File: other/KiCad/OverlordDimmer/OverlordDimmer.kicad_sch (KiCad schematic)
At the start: 103 parts, among them J1 Connector_Screw_Terminal_01x09, J2 USB_B, J3 DE15_Plug_HighDensity_Mountin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, J4 Connector_Screw_Terminal_01x09, J6 Conn_01x12_Pin, Q43 2SC4061KT146N, Q44 BC817, Q45 2SC4061KT146N, U12 4N35, U13 LM317_SOT-223, U14 ESP32S3-Wroom, U4 SN65HVD230

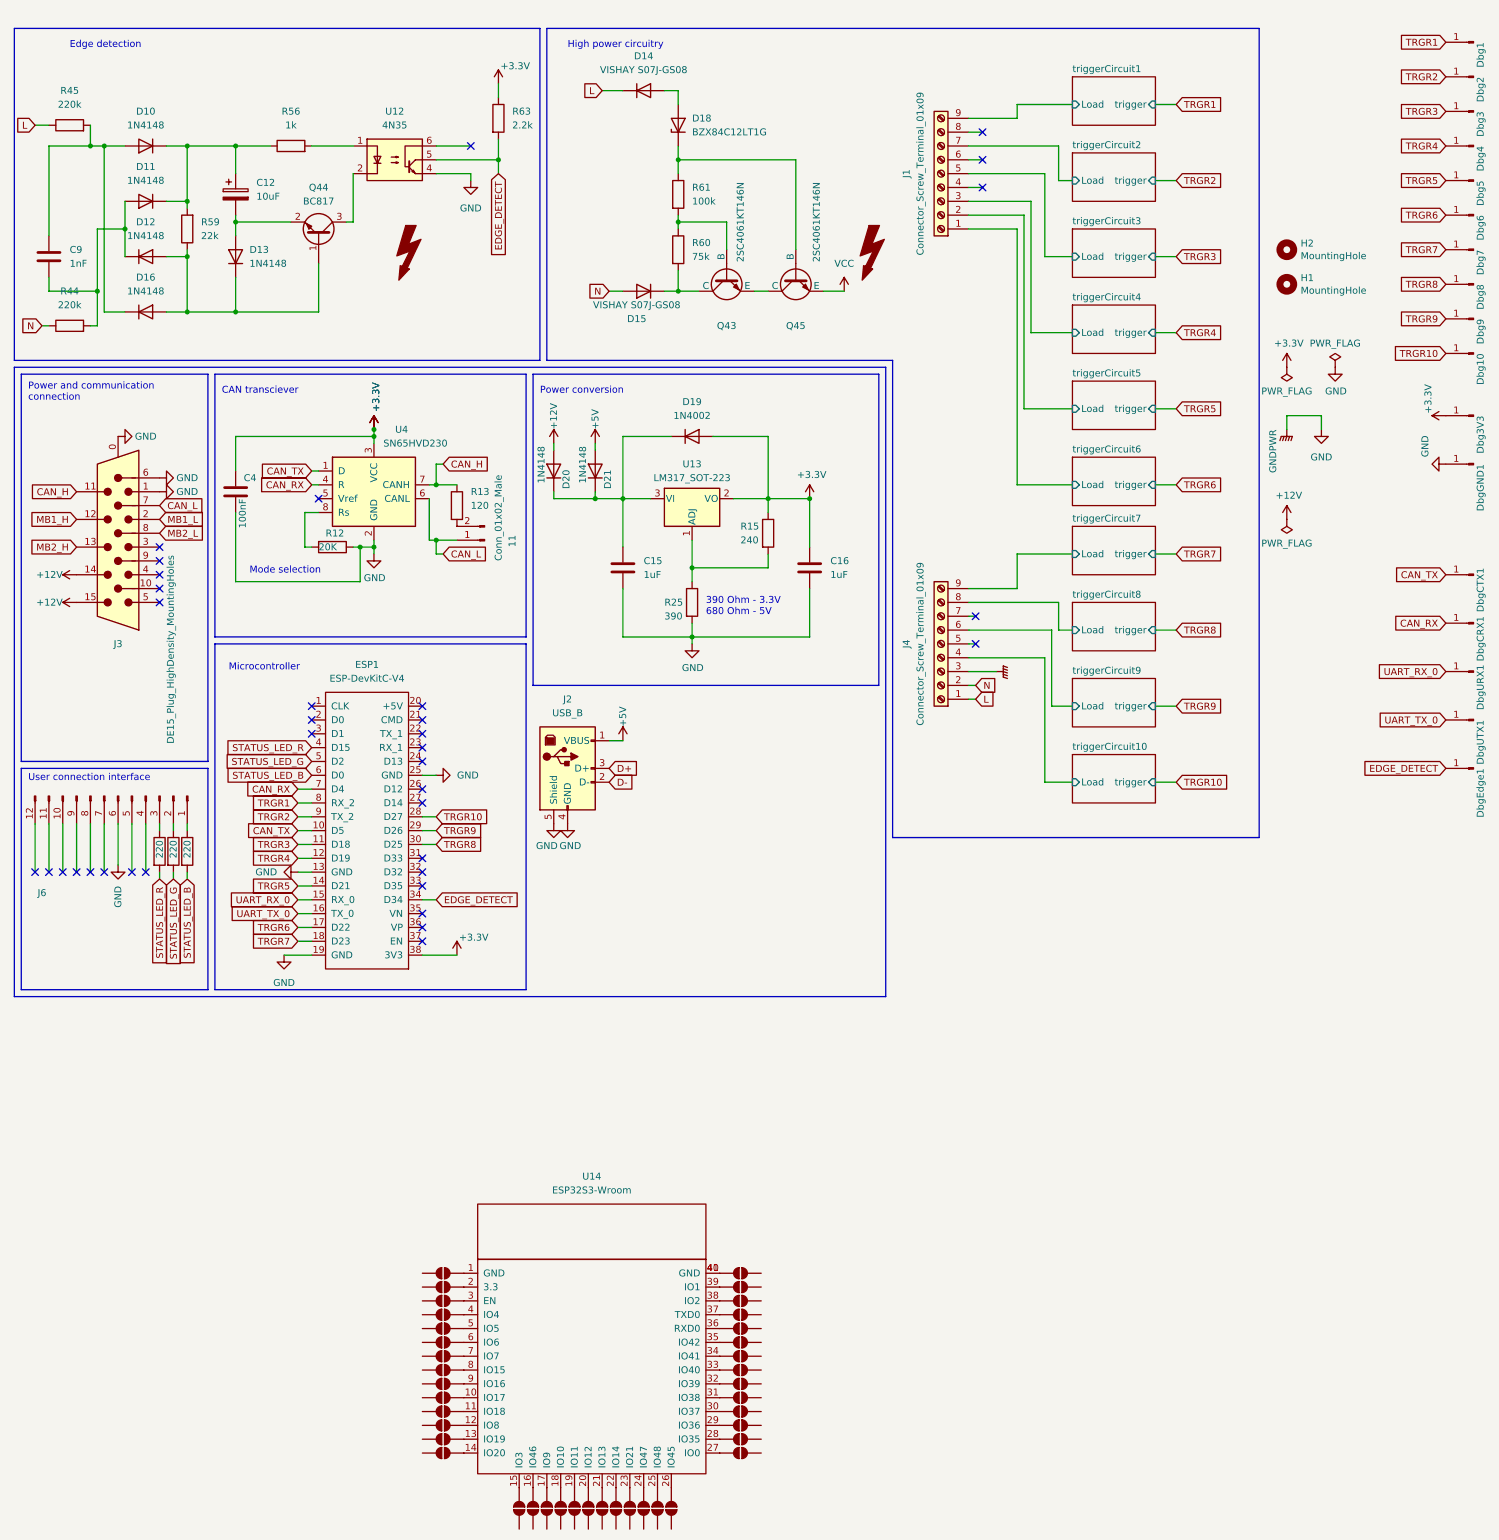
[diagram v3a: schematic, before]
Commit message: Modified for S3 migration Prepared PCB for final inspection
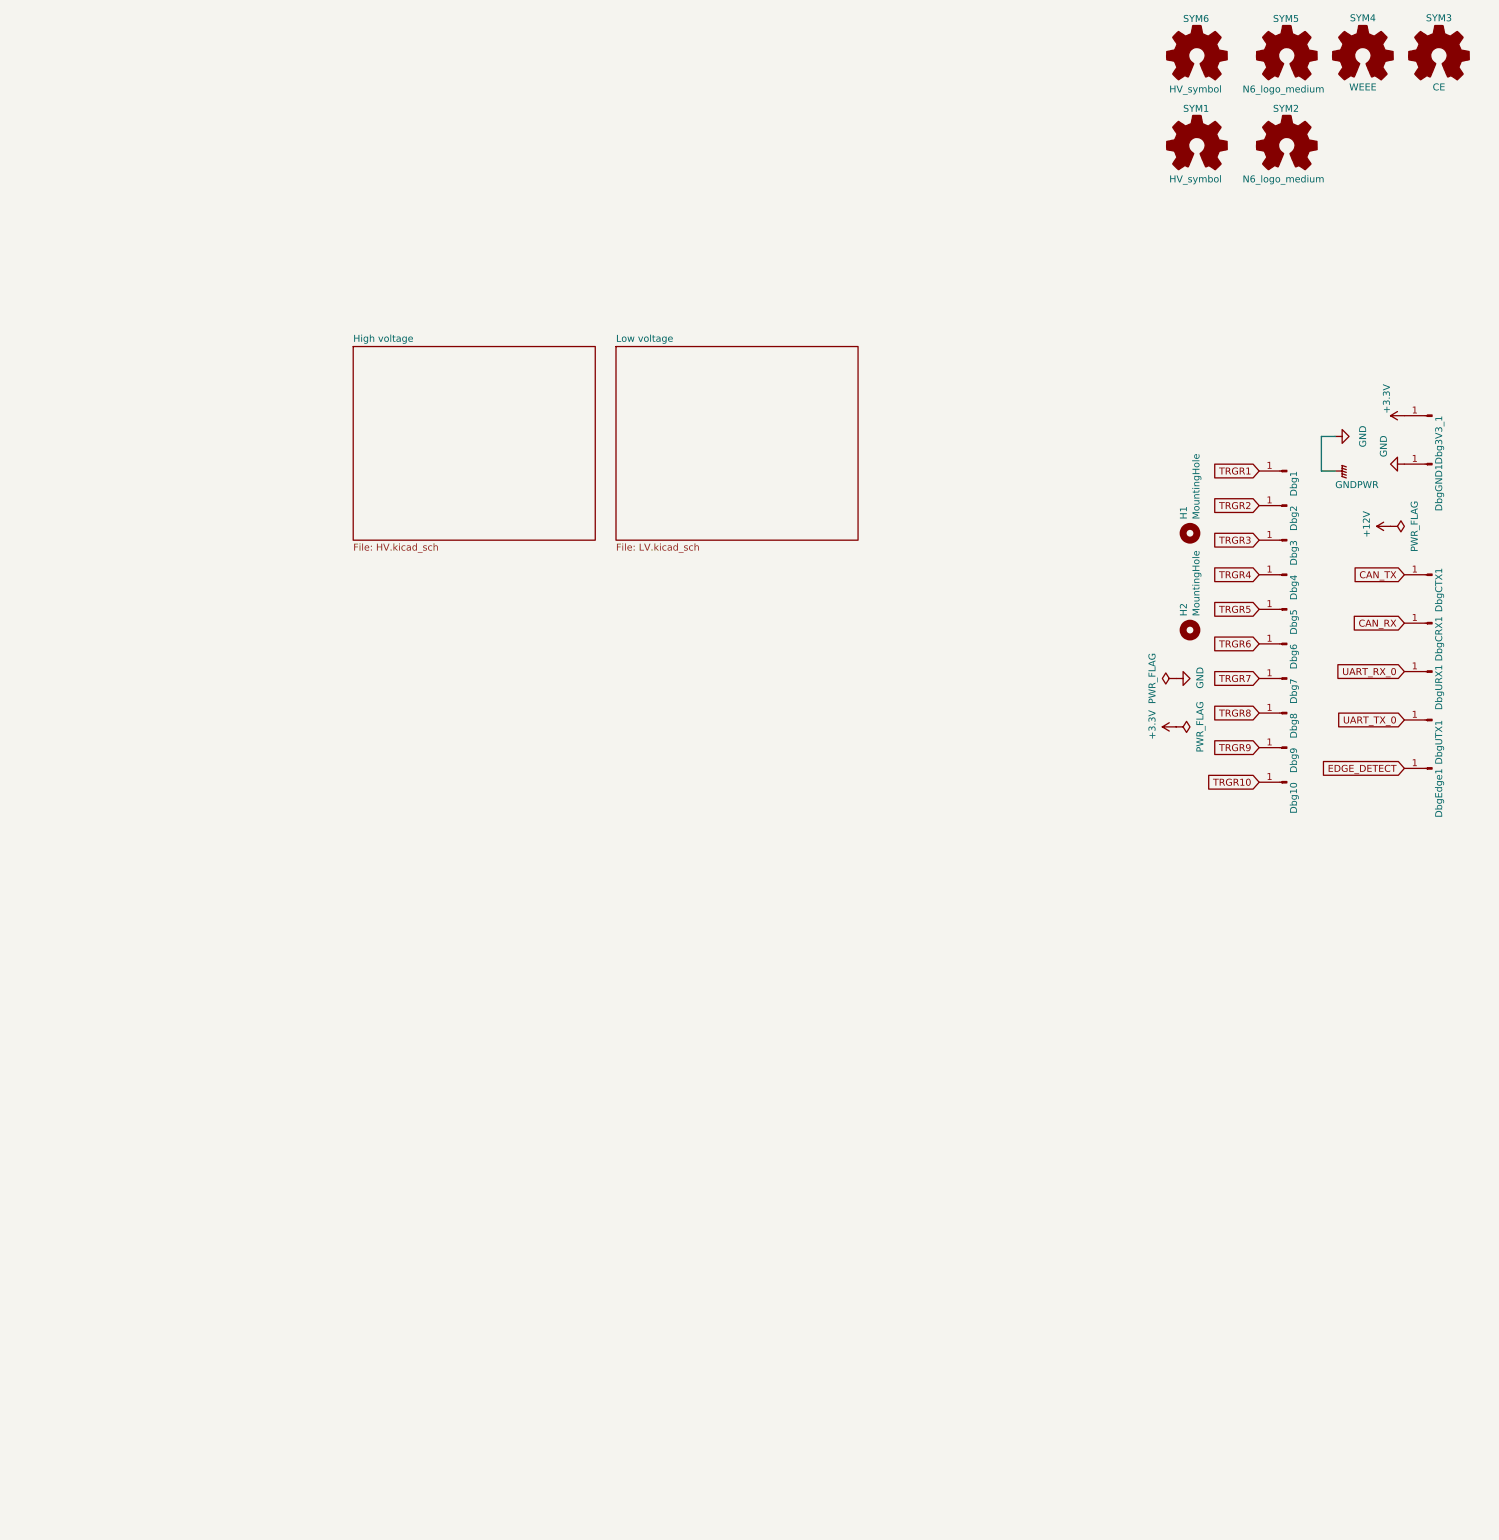
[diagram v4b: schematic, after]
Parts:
- removed 11: Conn_01x02_Male, Connector_PinHeader_2.54mm:PinHeader_1x02_P2.54mm_Vertical, symbol Connector:Conn_01x02_Pin
- removed C12: 10uF, Capacitor_THT:CP_Radial_D4.0mm_P1.50mm, symbol Device:C_Polarized
- removed C15, C16: 1uF, Capacitor_SMD:C_0402_1005Metric_Pad0.74x0.62mm_HandSolder, symbol Device:C
- removed C4: 100nF, Capacitor_THT:C_Disc_D6.0mm_W2.5mm_P5.00mm, symbol Device:C
- removed C9: 1nF, Capacitor_THT:C_Disc_D5.0mm_W2.5mm_P2.50mm, symbol Device:C
- removed D10, D11, D12, D13, D16, D20, D21: 1N4148, Diode_THT:D_DO-35_SOD27_P7.62mm_Horizontal, symbol Diode:1N4148
- removed D14, D15: VISHAY S07J-GS08, Diode_SMD:D_SMF, symbol Device:D
- removed D18: BZX84C12LT1G, Package_TO_SOT_SMD:SOT-23, symbol Diode:BZX84Cxx
- removed D19: 1N4002, Diode_THT:D_DO-41_SOD81_P2.54mm_Vertical_KathodeUp, symbol Device:D
- removed ESP1: ESP-DevKitC-V4, Overlord:ESP32-DevKitC-V4, symbol 74HC251D,653:ESP-DevKitC-V4
- removed J1, J4: Connector_Screw_Terminal_01x09, TerminalBlockCustom:TerminalBlock_9_5.08mm, symbol Overlord-cache:Connector_Screw_Terminal_01x09
- removed J2: USB_B, Connector_USB:USB_B_Lumberg_2411_02_Horizontal, symbol Connector:USB_B
- removed J3: DE15_Plug_HighDensity_MountingHoles, DSUB-15_Male_Horizontal_P2.77x2.84mm_EdgePinOffset7.70mm_Housed_MountingHolesOffset9.12mm, symbol Connector:DE15_Plug_HighDensity_MountingHoles
- removed J6: Conn_01x12_Pin, Connector_Molex:Molex_Picoflex_90325-0012_2x06_P1.27mm_Vertical, symbol Connector:Conn_01x12_Pin
- removed JP1, JP10, JP11, JP12, JP13, JP14, JP15, JP16, JP17, JP18, JP19, JP2, JP20, JP21, JP22, JP23, JP24, JP25, JP26, JP27, JP28, JP29, JP3, JP30, JP31, JP32, JP33, JP34, JP35, JP36, JP37, JP38, JP39, JP4, JP40, JP5, JP6, JP7, JP8, JP9: SolderJumper_2_Open, Jumper:SolderJumper-2_P1.3mm_Open_RoundedPad1.0x1.5mm, symbol Jumper:SolderJumper_2_Open
- removed Q43, Q45: 2SC4061KT146N, Package_TO_SOT_SMD:SC-59_Handsoldering, symbol Simulation_SPICE:NPN
- removed Q44: BC817, Package_TO_SOT_SMD:SOT-23, symbol Transistor_BJT:BC817
- removed R12: 20K, Resistor_SMD:R_0402_1005Metric_Pad0.72x0.64mm_HandSolder, symbol Device:R
- removed R13: 120, Resistor_SMD:R_0402_1005Metric_Pad0.72x0.64mm_HandSolder, symbol Device:R
- removed R15: 240, Resistor_SMD:R_1206_3216Metric_Pad1.30x1.75mm_HandSolder, symbol Device:R
- removed R25: 390, Resistor_SMD:R_1206_3216Metric_Pad1.30x1.75mm_HandSolder, symbol Device:R
- removed R44, R45: 220k, Resistor_SMD:R_0805_2012Metric_Pad1.20x1.40mm_HandSolder, symbol Device:R
- removed R56: 1k, Resistor_SMD:R_0805_2012Metric_Pad1.20x1.40mm_HandSolder, symbol Device:R
- removed R59: 22k, Resistor_SMD:R_0805_2012Metric_Pad1.20x1.40mm_HandSolder, symbol Device:R
- removed R60: 75k, Resistor_SMD:R_0805_2012Metric_Pad1.20x1.40mm_HandSolder, symbol Device:R
- removed R61: 100k, Resistor_SMD:R_0805_2012Metric_Pad1.20x1.40mm_HandSolder, symbol Device:R
- removed R63: 2.2k, Resistor_SMD:R_0805_2012Metric_Pad1.20x1.40mm_HandSolder, symbol Device:R
- removed R64, R65, R66: 220, Resistor_SMD:R_0805_2012Metric_Pad1.20x1.40mm_HandSolder, symbol Device:R
- removed U12: 4N35, Package_DIP:DIP-6_W7.62mm, symbol Isolator:4N35
- removed U13: LM317_SOT-223, Package_TO_SOT_SMD:SOT-223-3_TabPin2, symbol Regulator_Linear:LM317_SOT-223
- removed U14: ESP32S3-Wroom, PCM_Espressif:ESP32-S3-WROOM-1U, symbol ESP32S3-wroom:ESP32S3-Wroom
- removed U4: SN65HVD230, Package_SO:SOIC-8_3.9x4.9mm_P1.27mm, symbol Interface_CAN_LIN:SN65HVD230
- added SYM1, SYM6: HV_symbol, OverlordCommon:HV_symbol, symbol Graphic:Logo_Open_Hardware_Small
- added SYM2, SYM5: N6_logo_medium, OverlordCommon:Symbol_N6Industries_medium, symbol Graphic:Logo_Open_Hardware_Small
- added SYM3: CE, Symbol:CE-Logo_8.5x6mm_SilkScreen, symbol Graphic:Logo_Open_Hardware_Small
- added SYM4: WEEE, Symbol:WEEE-Logo_5.6x8mm_SilkScreen, symbol Graphic:Logo_Open_Hardware_Small
- H1, H2: now left out of the parts list
- renumbered Dbg3V3 to Dbg3V3_1
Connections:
- no-connect marks 36 -> 0
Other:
- removed sheet triggerCircuit1
- removed sheet triggerCircuit10
- removed sheet triggerCircuit2
- removed sheet triggerCircuit3
- removed sheet triggerCircuit4
- removed sheet triggerCircuit5
- removed sheet triggerCircuit6
- removed sheet triggerCircuit7
- removed sheet triggerCircuit8
- removed sheet triggerCircuit9
- added sheet High voltage (HV.kicad_sch)
- added sheet Low voltage (LV.kicad_sch)
- note removed: "390 Ohm - 3.3V 680 Ohm - 5V"
- note removed: "CAN transciever"
- note removed: "Edge detection"
- note removed: "High power circuitry"
- note removed: "Microcontroller"
- note removed: "Mode selection"
- note removed: "Power and communication connection"
- note removed: "Power conversion"
- note removed: "User connection interface"
- moved on the sheet: Dbg1, Dbg10, Dbg2, Dbg3, Dbg3V3_1, Dbg4, Dbg5, Dbg6, Dbg7, Dbg8, Dbg9, DbgCRX1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

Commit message: sent to production
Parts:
- renumbered SYM6 to SYM1, SYM5 to SYM2, SYM4 to SYM3, SYM3 to SYM4, SYM1 to SYM5, SYM2 to SYM6

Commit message: sent to production with fixes
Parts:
- removed H1, H2: MountingHole, MountingHole:MountingHole_3.5mm, symbol Mechanical:MountingHole
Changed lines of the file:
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@@
-	)
-	(symbol
-		(lib_id "Mechanical:MountingHole")
-		(at 229.87 127 90)
-		(unit 1)
-		(exclude_from_sim no)
-		(in_bom no)
-		(on_board yes)
-		(dnp no)
-		(property "Reference" "H2"
-			(at 228.7016 124.46 0)
-			(effects
-				(font
-					(size 1.27 1.27)
-				)
-				(justify left)
-			)
-		)
-		(property "Value" "MountingHole"
-			(at 231.013 124.46 0)
-			(effects
-				(font
-					(size 1.27 1.27)
-				)
-				(justify left)
-			)
-		)
-		(property "Footprint" "MountingHole:MountingHole_3.5mm"
-			(at 229.87 127 0)
-			(effects
-				(font
-					(size 1.27 1.27)
-				)
-				(hide yes)
-			)
-		)
-		(property "Datasheet" "~"
-			(at 229.87 127 0)
-			(effects
-				(font
-					(size 1.27 1.27)
-				)
-				(hide yes)
-			)
-		)
-		(property "Description" ""
-			(at 229.87 127 0)
-			(effects
-				(font
-					(size 1.27 1.27)
-				)
-				(hide yes)
-			)
-		)
-		(instances
-			(project "OverlordDimmer"
-				(path "/61f84ae7-a90a-49d4-ad4c-9c4f7abf6876"
-					(reference "H2")
-					(unit 1)
-				)
-			)
-		)
 	)
 	(symbol
@@
 					(unit 1)
 				)
-			)
-		)
-	)
-	(symbol
-		(lib_id "Mechanical:MountingHole")
-		(at 229.87 109.22 90)
-		(unit 1)
-		(exclude_from_sim no)
-		(in_bom no)
-		(on_board yes)
-		(dnp no)
-		(property "Reference" "H1"
-			(at 228.7016 106.68 0)
-			(effects
-				(font
-					(size 1.27 1.27)
-				)
-				(justify left)
-			)
-		)
-		(property "Value" "MountingHole"
-			(at 231.013 106.68 0)
-			(effects
-				(font
-					(size 1.27 1.27)
-				)
-				(justify left)
-			)
-		)
-		(property "Footprint" "MountingHole:MountingHole_3.5mm"
-			(at 229.87 109.22 0)
-			(effects
-				(font
-					(size 1.27 1.27)
-				)
-				(hide yes)
-			)
-		)
-		(property "Datasheet" "~"
-			(at 229.87 109.22 0)
-			(effects
-				(font
-					(size 1.27 1.27)
-				)
-				(hide yes)
-			)
-		)
-		(property "Description" ""
-			(at 229.87 109.22 0)
-			(effects
-				(font
-					(size 1.27 1.27)
-				)
-				(hide yes)
-			)
-		)
-		(instances
-			(project "OverlordDimmer"
-				(path "/61f84ae7-a90a-49d4-ad4c-9c4f7abf6876"
-					(reference "H1")
-					(unit 1)
-				)

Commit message: Sent for PCB production, ver 1.2 rev A
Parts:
- removed SYM4: CE, Symbol:CE-Logo_8.5x6mm_SilkScreen, symbol Graphic:Logo_Open_Hardware_Small
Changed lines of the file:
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@@
-	)
-	(symbol
-		(lib_id "Graphic:Logo_Open_Hardware_Small")
-		(at 275.59 21.59 0)
-		(unit 1)
-		(exclude_from_sim no)
-		(in_bom no)
-		(on_board yes)
-		(dnp no)
-		(fields_autoplaced yes)
-		(property "Reference" "SYM4"
-			(at 275.59 14.605 0)
-			(effects
-				(font
-					(size 1.27 1.27)
-				)
-			)
-		)
-		(property "Value" "CE"
-			(at 275.59 27.305 0)
-			(effects
-				(font
-					(size 1.27 1.27)
-				)
-			)
-		)
-		(property "Footprint" "Symbol:CE-Logo_8.5x6mm_SilkScreen"
-			(at 275.59 21.59 0)
-			(effects
-				(font
-					(size 1.27 1.27)
-				)
-				(hide yes)
-			)
-		)
-		(property "Datasheet" "~"
-			(at 275.59 21.59 0)
-			(effects
-				(font
-					(size 1.27 1.27)
-				)
-				(hide yes)
-			)
-		)
-		(property "Description" "Open Hardware logo, small"
-			(at 275.59 21.59 0)
-			(effects
-				(font
-					(size 1.27 1.27)
-				)
-				(hide yes)
-			)
-		)
-		(instances
-			(project ""
-				(path "/61f84ae7-a90a-49d4-ad4c-9c4f7abf6876"
-					(reference "SYM4")
-					(unit 1)
-				)
-			)
-		)
 	)
 	(symbol
